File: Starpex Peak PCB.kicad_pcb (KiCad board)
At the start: 2 copper layers, 83.2 x 59.7 mm, 5 parts

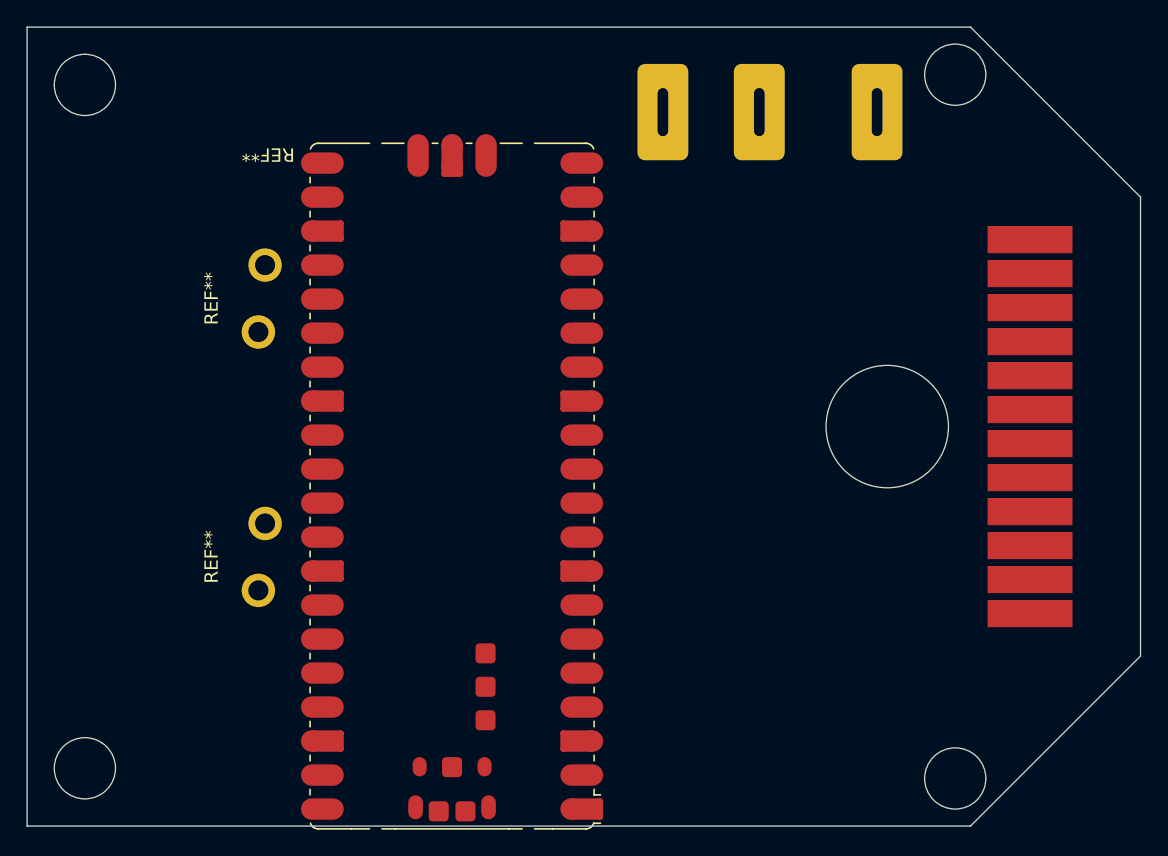
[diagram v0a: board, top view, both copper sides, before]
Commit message: Peak PCB 1.0
All traces ready. Now need to make daughterboard for RPi Pico
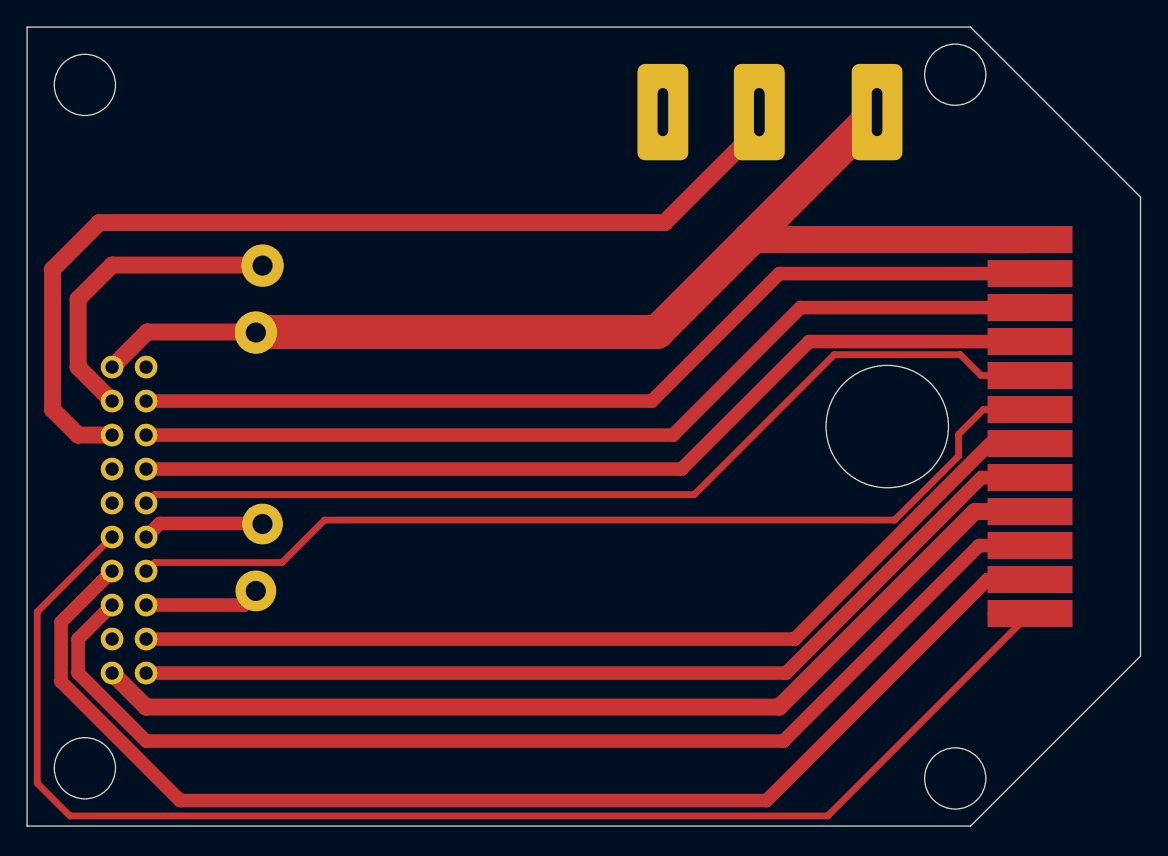
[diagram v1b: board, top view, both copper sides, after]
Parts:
- removed REF**: KW11, Custom Footprints:KW11
- removed REF**: GH, Custom Footprints:GH
- removed REF**: RaspberryPi_Pico_SMD, Module:RaspberryPi_Pico_SMD
- removed REF** (x2): SW_Alps_Matias, PCM_Switch_Keyboard_Alps_Matias:SW_Alps_Matias
- added J1: Conn_01x12_Pin, Custom Footprints:GH, F.Cu at (167.6, 122.8)
- added J2: Conn_01x20_Pin, Connector_PinHeader_2.54mm:PinHeader_2x10_P2.54mm_Vertical, B.Cu at (101.6, 118.1)
- added SW1: SW_SPDT_321, Custom Footprints:KW11, B.Cu at (156.2, 99.1)
- added SW2: SW_Push, PCM_Switch_Keyboard_Alps_Matias:SW_Alps_Matias, B.Cu at (114.3, 113.0)
- added SW3: SW_Push, PCM_Switch_Keyboard_Alps_Matias:SW_Alps_Matias, B.Cu at (114.3, 132.3)
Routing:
- net Net-(J1-Pin_12): track 0.00 -> 104.7 mm
- net Net-(J1-Pin_11): track 0.00 -> 92.7 mm
- net Net-(J1-Pin_1): track 0.00 -> 86.0 mm
- net Net-(J1-Pin_10): track 0.00 -> 85.4 mm
- net Net-(J1-Pin_9): track 0.00 -> 75.7 mm
- net Net-(J2-Pin_6): track 0.00 -> 74.1 mm
- net Net-(J1-Pin_6): track 0.00 -> 72.2 mm
- net Net-(J1-Pin_8): track 0.00 -> 72.1 mm
- net Net-(J1-Pin_7): track 0.00 -> 72.1 mm
- net Net-(J1-Pin_5): track 0.00 -> 71.3 mm
- net Net-(J1-Pin_4): track 0.00 -> 70.0 mm
- net Net-(J1-Pin_3): track 0.00 -> 70.0 mm
- net Net-(J1-Pin_2): track 0.00 -> 70.0 mm
- net Net-(J2-Pin_4): track 0.00 -> 23.7 mm
- net Net-(J2-Pin_11): track 0.00 -> 9.31 mm
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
